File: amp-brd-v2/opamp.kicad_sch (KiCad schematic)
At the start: 15 parts, among them U1 OPA547F, U2 INA233

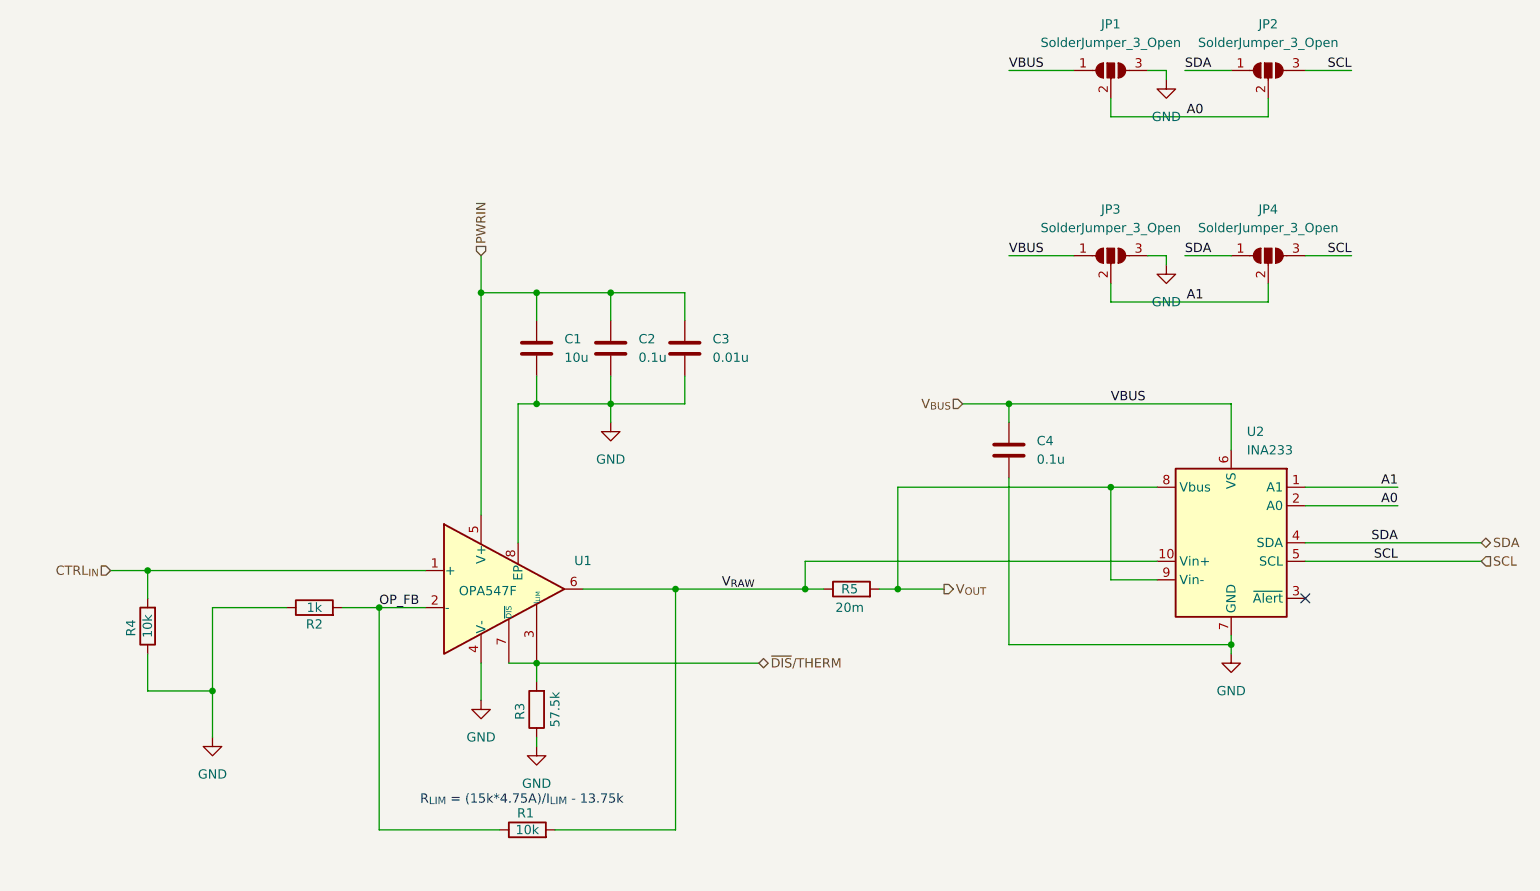
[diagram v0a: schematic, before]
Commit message: Stackable AMP
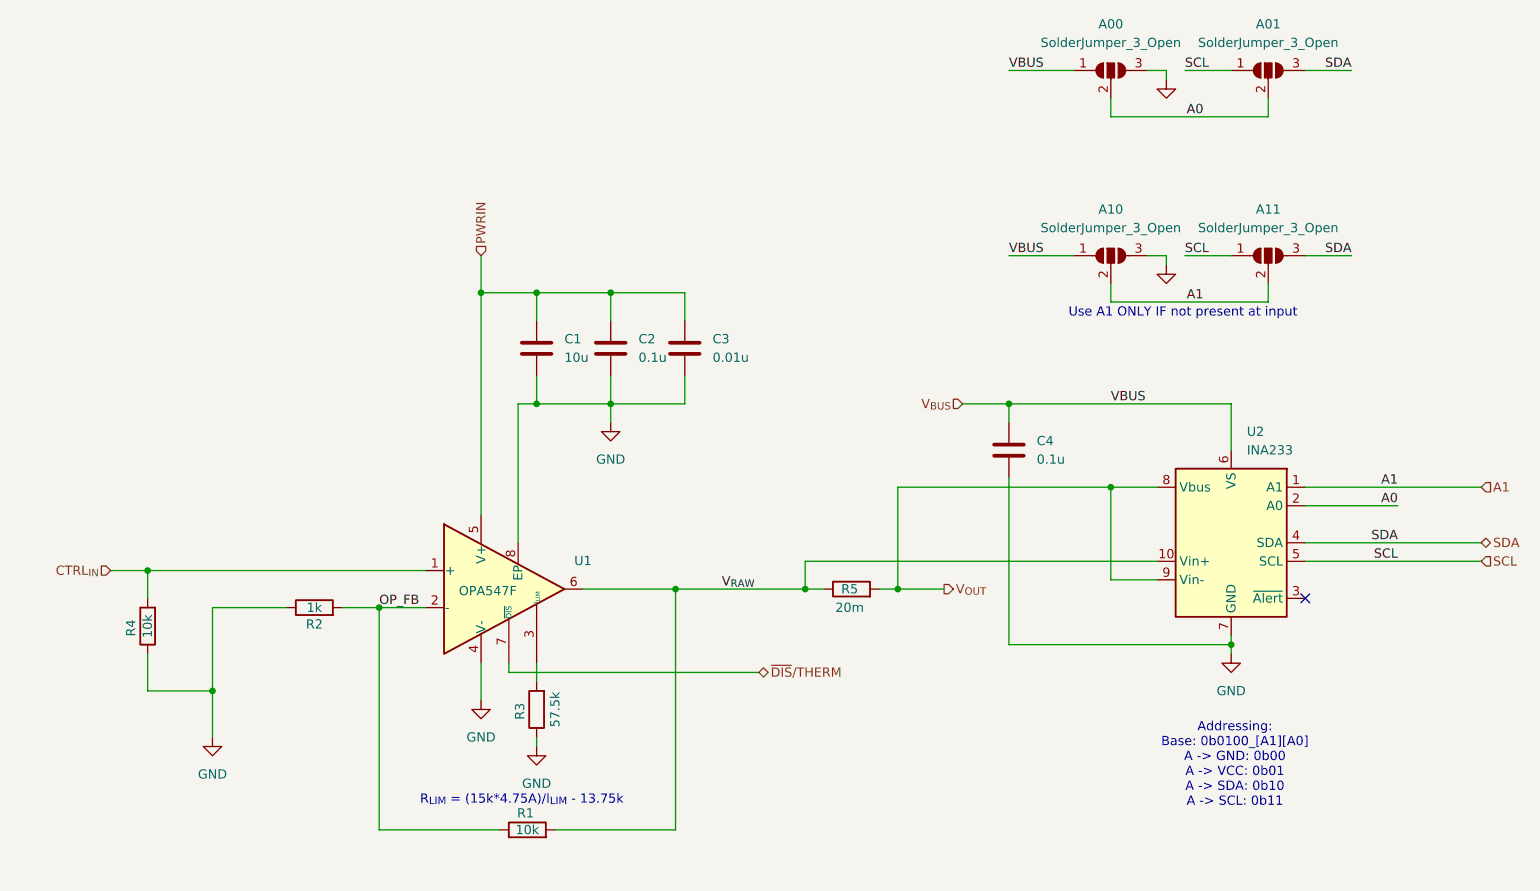
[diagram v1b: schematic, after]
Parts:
- renumbered JP1 to A00, JP2 to A01, JP3 to A10, JP4 to A11
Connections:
- net SCL: now also A01.1 (A), A11.1 (A); no longer A01.3 (B), A11.3 (B)
- net SDA: now also A01.3 (B), A11.3 (B); no longer A01.1 (A), A11.1 (A)
- net ~{DIS}/THERM: no longer R3.2, U1.3 (I_{LIM})
- new net: R3.2, U1.3 (I_{LIM})
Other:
- note added: "Addressing: Base: 0b0100_[A1][A0] A -> GND: 0b00 A -> VCC: 0b01 A -> SDA: 0b10 A -> SCL: 0b11"
- note added: "Use A1 ONLY IF not present at input"
- company: (none) -> LoCSST / UMass Lowell
- title: (none) -> ${PRJ_TITLE}
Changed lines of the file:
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@@
 	(generator_version "9.0")
 	(paper "A4")
+	(title_block
+		(title "${PRJ_TITLE}")
+		(date "2025-11-29")
+		(rev "${BOARD_REV}")
+		(company "LoCSST / UMass Lowell")
+		(comment 1 "Designer: ${DESIGNER}")
+		(comment 2 "Reviwer: ${REVIEWER}")
+	)
+	(text "Use A1 ONLY IF not present at input"
+		(exclude_from_sim no)
+		(at 209.296 75.184 0)
+		(effects
+			(font
+				(size 1.27 1.27)
+			)
+		)
+	)
+	(text "Addressing:\nBase: 0b0100_[A1][A0]\nA -> GND: 0b00\nA -> VCC: 0b01\nA -> SDA: 0b10\nA -> SCL: 0b11"
+		(exclude_from_sim no)
+		(at 216.408 137.16 0)
+		(effects
+			(font
+				(size 1.27 1.27)
+			)
+		)
+	)
 	(text "R_{LIM} = (15k*4.75A)/I_{LIM} - 13.75k"
 		(exclude_from_sim no)
@@
 	)
 	(junction
-		(at 120.65 123.19)
-		(diameter 0)
-		(color 0 0 0 0)
-	)
-	(junction
 		(at 199.39 99.06)
 		(diameter 0)
@@
 	(wire
 		(pts
-			(xy 120.65 123.19) (xy 151.13 123.19)
+			(xy 116.84 124.46) (xy 151.13 124.46)
 		)
 		(stroke
@@
 	(wire
 		(pts
-			(xy 116.84 123.19) (xy 120.65 123.19)
-		)
-		(stroke
-			(width 0)
-			(type default)
-		)
-	)
-	(wire
-		(pts
 			(xy 99.06 115.57) (xy 105.41 115.57)
 		)
@@
 	(wire
 		(pts
+			(xy 116.84 124.46) (xy 116.84 123.19)
+		)
+		(stroke
+			(width 0)
+			(type default)
+		)
+	)
+	(wire
+		(pts
 			(xy 67.31 121.92) (xy 67.31 127)
 		)
@@
 	(wire
 		(pts
-			(xy 226.06 99.06) (xy 238.76 99.06)
+			(xy 226.06 99.06) (xy 250.19 99.06)
 		)
 		(stroke
@@
 	)
 	(label "SCL"
-		(at 232.41 67.31 180)
+		(at 209.55 67.31 0)
 		(effects
 			(font
 				(size 1.27 1.27)
 			)
-			(justify right bottom)
+			(justify left bottom)
 		)
 	)
@@
 	)
 	(label "SDA"
-		(at 209.55 67.31 0)
+		(at 232.41 67.31 180)
 		(effects
 			(font
 				(size 1.27 1.27)
 			)
-			(justify left bottom)
+			(justify right bottom)
 		)
 	)
@@
 	)
 	(label "SDA"
+		(at 232.41 41.91 180)
+		(effects
+			(font
+				(size 1.27 1.27)
+			)
+			(justify right bottom)
+		)
+	)
+	(label "SCL"
 		(at 209.55 41.91 0)
 		(effects
@@
 			)
 			(justify left bottom)
-		)
-	)
-	(label "SCL"
-		(at 232.41 41.91 180)
-		(effects
-			(font
-				(size 1.27 1.27)
-			)
-			(justify right bottom)
 		)
 	)
@@
 		)
 	)
+	(hierarchical_label "A1"
+		(shape input)
+		(at 250.19 99.06 0)
+		(effects
+			(font
+				(size 1.27 1.27)
+			)
+			(justify left)
+		)
+	)
 	(hierarchical_label "SDA"
 		(shape bidirectional)
@@
 	(hierarchical_label "~{DIS}{slash}THERM"
 		(shape bidirectional)
-		(at 151.13 123.19 0)
+		(at 151.13 124.46 0)
 		(effects
 			(font
@@
 					(size 1.27 1.27)
 				)
+				(hide yes)
 			)
 		)
@@
 		(dnp no)
 		(fields_autoplaced yes)
-		(property "Reference" "JP3"
+		(property "Reference" "A10"
 			(at 199.39 60.96 0)
 			(effects
@@
 			(project "amplifier-brd"
 				(path "/4a199ccc-be1f-4132-9551-a46e36599bcb/f2b7aa34-9911-40d3-beee-632deab3d3cc"
-					(reference "JP3")
+					(reference "A10")
 					(unit 1)
 				)
@@
 		(dnp no)
 		(fields_autoplaced yes)
-		(property "Reference" "JP2"
+		(property "Reference" "A01"
 			(at 220.98 35.56 0)
 			(effects
@@
 			(project "amplifier-brd"
 				(path "/4a199ccc-be1f-4132-9551-a46e36599bcb/f2b7aa34-9911-40d3-beee-632deab3d3cc"
-					(reference "JP2")
+					(reference "A01")
 					(unit 1)
 				)
@@
 		(dnp no)
 		(fields_autoplaced yes)
-		(property "Reference" "JP1"
+		(property "Reference" "A00"
 			(at 199.39 35.56 0)
 			(effects
@@
 			(project ""
 				(path "/4a199ccc-be1f-4132-9551-a46e36599bcb/f2b7aa34-9911-40d3-beee-632deab3d3cc"
-					(reference "JP1")
+					(reference "A00")
 					(unit 1)
 				)
@@
 		(dnp no)
 		(fields_autoplaced yes)
-		(property "Reference" "JP4"
+		(property "Reference" "A11"
 			(at 220.98 60.96 0)
 			(effects
@@
 			(project "amplifier-brd"
 				(path "/4a199ccc-be1f-4132-9551-a46e36599bcb/f2b7aa34-9911-40d3-beee-632deab3d3cc"
-					(reference "JP4")
+					(reference "A11")
 					(unit 1)
 				)
@@
 					(size 1.27 1.27)
 				)
-			)
-		)
+				(hide yes)
+			)
+		)

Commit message: Finished mezzanine layout
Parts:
- added C5: 0.01u, Capacitor_SMD:C_0805_2012Metric, symbol Device:C
- added JP1: SolderJumper_2_Open, Jumper:SolderJumper-2_P1.3mm_Open_RoundedPad1.0x1.5mm, symbol Jumper:SolderJumper_2_Open
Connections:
- net GND: now also C5.2
- net ~{DIS}/THERM: now also C5.1, JP1.2 (B); no longer U1.7 (~{DIS})
- net ILIM: now reaches R3.2, U1.3 (I_{LIM})
- new net STAT_PIN: JP1.1 (A), U1.7 (~{DIS})
